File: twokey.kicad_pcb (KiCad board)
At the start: 2 copper layers, 52.1 x 38.1 mm, 10 parts, among them J1 12401610E4#2A, U1 ATSAMD21E18A-A, U2 MCP1700-3302E_SOT23

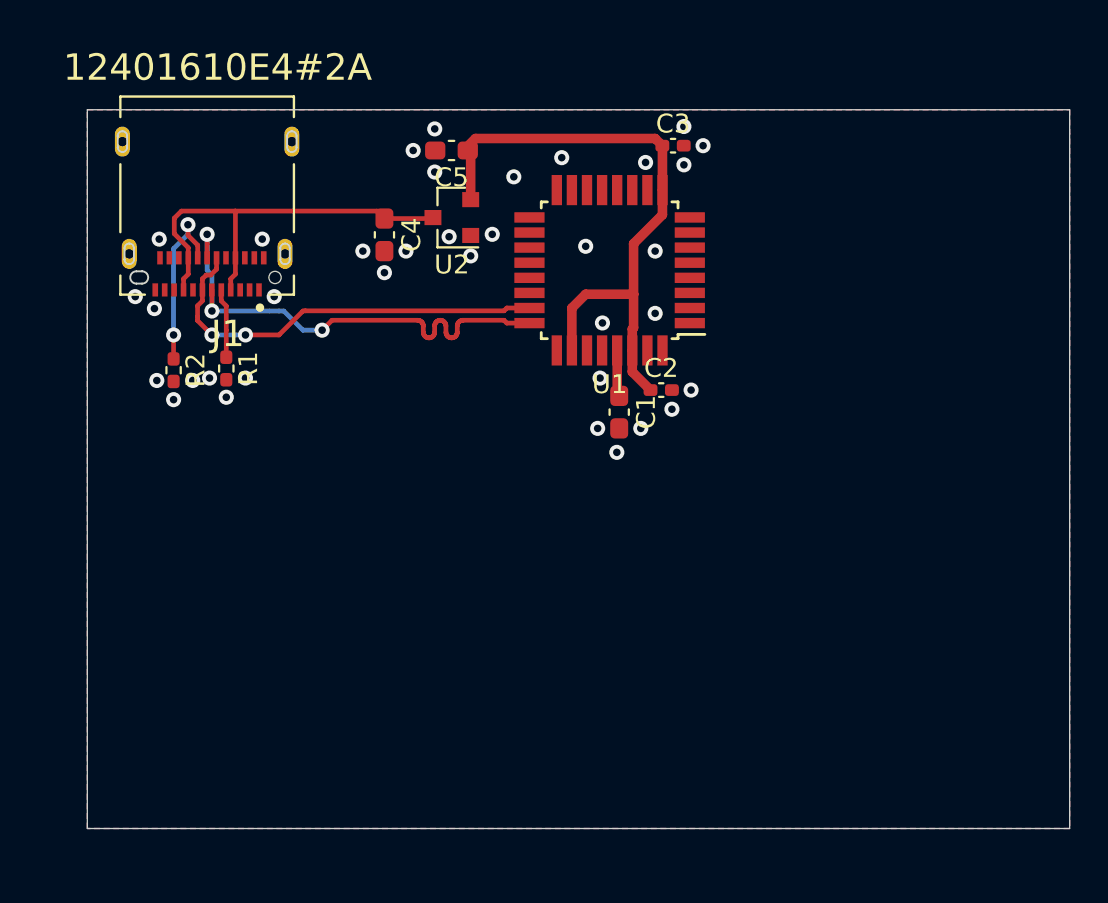
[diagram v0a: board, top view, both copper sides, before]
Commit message: added key switches
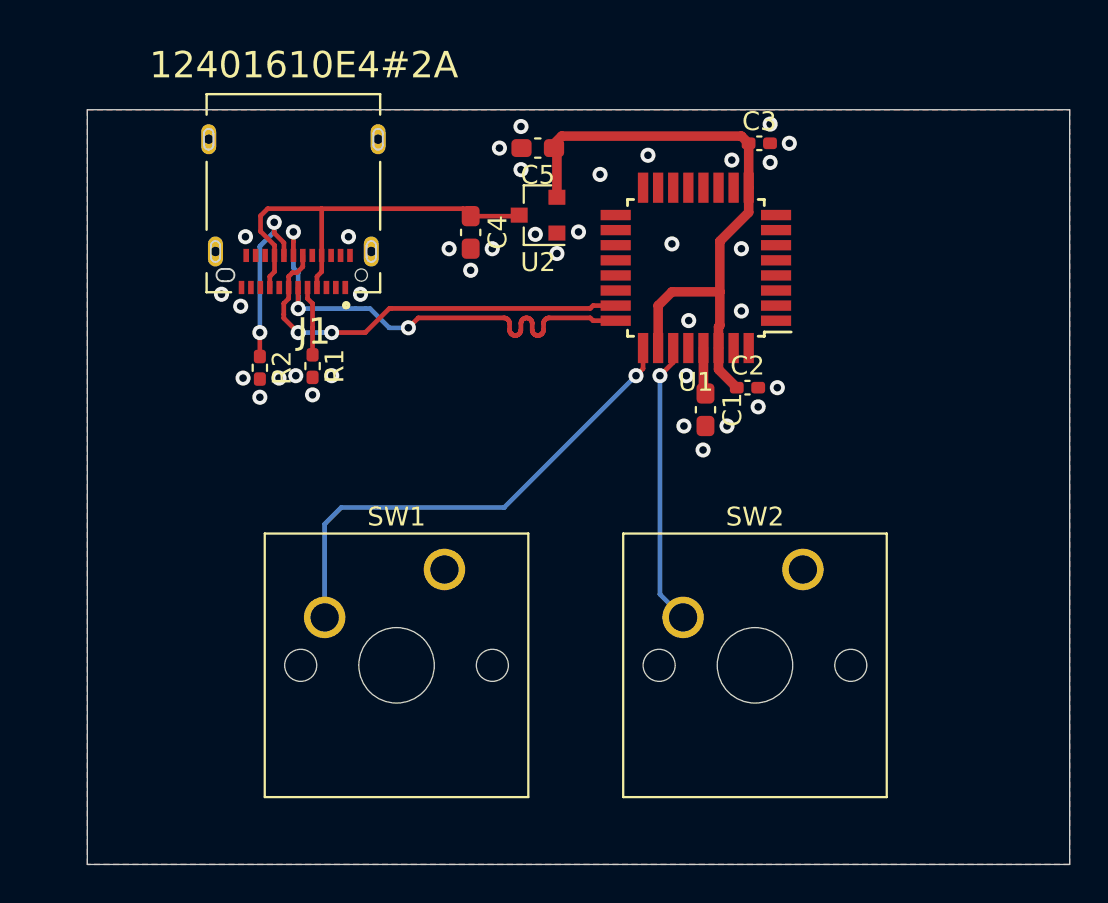
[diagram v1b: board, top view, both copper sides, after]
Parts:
- added SW1: SW_SPST, Button_Switch_Keyboard:SW_Cherry_MX_1.00u_PCB, F.Cu at (134.5, 112.0)
- added SW2: SW_SPST, Button_Switch_Keyboard:SW_Cherry_MX_1.00u_PCB, F.Cu at (153.5, 112.0)
- moved C1 4.57 mm to (148.3, 103.5)
- moved C2 4.57 mm to (150.6, 102.4)
- moved C3 4.57 mm to (151.2, 89.4)
- moved C5 4.57 mm to (139.4, 89.7)
- moved J1 4.57 mm to (126.5, 96.4)
- moved R2 4.57 mm to (124.7, 101.3)
- moved U1 4.57 mm to (147.8, 96.0)
- moved U2 4.57 mm to (139.5, 93.2)
- moved R1 4.57 mm to (127.5, 101.2)
- moved C4 4.57 mm to (135.9, 94.1)
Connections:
- U1 pad 25: Net-(U1-Pad25) -> KEY1
- U1 pad 27: Net-(U1-Pad27) -> KEY2
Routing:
- net KEY1: track 0.00 -> 26.3 mm, vias 0 -> 1
- net KEY2: track 0.00 -> 15.1 mm, vias 0 -> 1
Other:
- board size 52.1 x 38.1 mm -> 52.1 x 40 mm

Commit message: ordered pcb
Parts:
- added D1: BB-2020BGR-TRB, twokey:LED_BB-2020BGR-TRB, B.Cu at (-9.70, 10.1)
- added D2: BB-2020BGR-TRB, twokey:LED_BB-2020BGR-TRB, B.Cu at (9.55, 10.1)
- added J2: Conn_02x03_Odd_Even, twokey:TC2030-IDC-NL, F.Cu at (-21.7, -6.07)
- added REF**: MountingHole_3.2mm_M3, MountingHole:MountingHole_3.2mm_M3, F.Cu at (-21.3, -16.2)
- added REF**: MountingHole_3.2mm_M3, MountingHole:MountingHole_3.2mm_M3, F.Cu at (-21.3, 16.2)
- added REF**: MountingHole_3.2mm_M3, MountingHole:MountingHole_3.2mm_M3, F.Cu at (21.3, 16.2)
- added U3: PTS526_SK15_SMTR2_LFS, twokey:PTS526 SK15 SMTR2 LFS, B.Cu at (20.0, -15.0)
- J1: footprint 12401610E4_2A:AMPHENOL_12401610E4#2A -> Digi-Key:AMPHENOL_12401610E4#2A
- SW1, SW2: moved to B.Cu
- U1: footprint Package_QFP:TQFP-32_7x7mm_P0.8mm -> Package_DFN_QFN:QFN-32-1EP_5x5mm_P0.5mm_EP3.6x3.6mm
- moved C2 201.1 mm to (-13.8, -13.4), turned to 180 degrees
- moved SW2 200.0 mm to (-12.2, 0.00), turned to 180 degrees
- moved C1 200.0 mm to (-12.2, -15.6), turned to 90 degrees
- moved U1 191.8 mm to (-12.3, -9.58), turned to 0 degrees
- moved C3 189.9 mm to (-13.3, -5.61)
- moved R2 174.5 mm to (-6.27, -14.1)
- moved SW1 169.7 mm to (7.00, 0.00), turned to 180 degrees
- moved U2 167.2 mm to (5.13, -6.28), turned to 90 degrees
- moved R1 166.9 mm to (1.45, -8.09)
- moved J1 166.1 mm to (0.00, -11.2)
- moved C4 165.9 mm to (5.94, -8.94), turned to 0 degrees
- moved C5 161.8 mm to (6.99, -3.33), turned to 0 degrees
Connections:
- U1 pad 1: Net-(U1-Pad1) -> BUTTON
- U1 pad 15: Net-(U1-Pad15) -> KEY2
- U1 pad 16: Net-(U1-Pad16) -> KEY1
- U1 pad 25: KEY1 -> Net-(U1-Pad25)
- U1 pad 26: +3V3 -> ~RESET
- U1 pad 27: KEY2 -> Net-(U1-Pad27)
- U1 pad 31: Net-(U1-Pad31) -> SWCLK
- U1 pad 32: Net-(U1-Pad32) -> SWDIO
- U1 pad 7: Net-(U1-Pad7) -> LED_DI
- U1 pad 8: Net-(U1-Pad8) -> LED_CI
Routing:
- net VBUS: track 22.6 -> 72.2 mm, vias 0 -> 3
- net BUTTON: track 0.00 -> 46.1 mm, vias 0 -> 3
- net LED_DI: track 0.00 -> 26.9 mm, vias 0 -> 1
- net ~RESET: track 0.00 -> 26.7 mm, vias 0 -> 2
- net LED_CI: track 0.00 -> 24.0 mm, vias 0 -> 1
- net Net-(D1-Pad6): track 0.00 -> 17.5 mm
- net Net-(D1-Pad1): track 0.00 -> 17.5 mm
- net SWCLK: track 0.00 -> 15.4 mm
- net +3V3: track 33.7 -> 46.5 mm, vias 0 -> 2
- net SWDIO: track 0.00 -> 10.8 mm
- net D-: track 22.4 -> 12.6 mm, vias 2 -> 0
- net D+: track 26.8 -> 19.4 mm, vias 3 -> 4
- net KEY1: track 26.3 -> 31.4 mm
- net Net-(J1-PadB5): track 9.65 -> 7.39 mm, vias 2 -> 0
- net Net-(J1-PadA5): track 3.68 -> 2.19 mm
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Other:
- board size 52.1 x 40 mm -> 50 x 40 mm
- net class +3.3V: trace_width 0.508 -> 0.25
- net class VBUS added: clearance 0.2, trace_width 0.25, via_dia 0.8, via_drill 0.4
